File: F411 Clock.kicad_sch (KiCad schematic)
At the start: 0 parts

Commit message: SCH Save: 4 files changed F411 Clock.kicad_prl 105/0/0 F411 Clock.kicad_pro 429/0/1 F411 Clock.kicad_sch 1893/0/3 ~F411 Clock.kicad_sch.lck 1/0/0
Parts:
- added DS1: WC1602A, Display:WC1602A, symbol Display_Character:WC1602A
- added U1: STM32F411CCUx, Package_DFN_QFN:QFN-48-1EP_7x7mm_P0.5mm_EP5.15x5.15mm, symbol MCU_ST_STM32F4:STM32F411CCUx
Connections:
- new net: U1.23 (VSS), U1.35 (VSS), U1.47 (VSS), U1.49 (VSS)

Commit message: SCH Save: 2 files changed F411 Clock.kicad_pro 0/0/1 F411 Clock.kicad_sch 898/0/6
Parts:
- added J1: USB_C_Receptacle_USB2.0_16P, Connector_USB:USB_C_Receptacle_HCTL_HC-TYPE-C-16P-01A, symbol Connector:USB_C_Receptacle_USB2.0_16P
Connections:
- new net: J1.A1 (GND), J1.A12 (GND), J1.B1 (GND), J1.B12 (GND)
- new net: J1.A4 (VBUS), J1.A9 (VBUS), J1.B4 (VBUS), J1.B9 (VBUS)
- new net: J1.A6 (D+), J1.B6 (D+)
- new net: J1.A7 (D-), J1.B7 (D-)
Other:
- moved on the sheet: DS1
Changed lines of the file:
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@@
 	(generator_version "10.0")
 	(paper "A4")
+	(wire
+		(pts
+			(xy 55.88 81.28) (xy 55.88 83.82)
+		)
+		(stroke
+			(width 0)
+			(type default)
+		)
+	)
+	(wire
+		(pts
+			(xy 53.34 76.2) (xy 55.88 76.2)
+		)
+		(stroke
+			(width 0)
+			(type default)
+		)
+	)
+	(wire
+		(pts
+			(xy 53.34 81.28) (xy 55.88 81.28)
+		)
+		(stroke
+			(width 0)
+			(type default)
+		)
+	)
+	(wire
+		(pts
+			(xy 55.88 76.2) (xy 55.88 78.74)
+		)
+		(stroke
+			(width 0)
+			(type default)
+		)
+	)
+	(wire
+		(pts
+			(xy 53.34 83.82) (xy 55.88 83.82)
+		)
+		(stroke
+			(width 0)
+			(type default)
+		)
+	)
+	(wire
+		(pts
+			(xy 53.34 78.74) (xy 55.88 78.74)
+		)
+		(stroke
+			(width 0)
+			(type default)
+		)
+	)
+	(symbol
+		(lib_id "Connector:USB_C_Receptacle_USB2.0_16P")
+		(at 38.1 78.74 0)
+		(unit 1)
+		(body_style 1)
+		(exclude_from_sim no)
+		(in_bom yes)
+		(on_board yes)
+		(in_pos_files yes)
+		(dnp no)
+		(fields_autoplaced yes)
+		(property "Reference" "J1"
+			(at 38.1 55.88 0)
+			(show_name no)
+			(do_not_autoplace no)
+			(effects
+				(font
+					(size 1.27 1.27)
+				)
+			)
+		)
+		(property "Value" "USB_C_Receptacle_USB2.0_16P"
+			(at 38.1 58.42 0)
+			(show_name no)
+			(do_not_autoplace no)
+			(effects
+				(font
+					(size 1.27 1.27)
+				)
+			)
+		)
+		(property "Footprint" "Connector_USB:USB_C_Receptacle_HCTL_HC-TYPE-C-16P-01A"
+			(at 41.91 78.74 0)
+			(hide yes)
+			(show_name no)
+			(do_not_autoplace no)
+			(effects
+				(font
+					(size 1.27 1.27)
+				)
+			)
+		)
+		(property "Datasheet" "https://www.usb.org/sites/default/files/documents/usb_type-c.zip"
+			(at 41.91 78.74 0)
+			(hide yes)
+			(show_name no)
+			(do_not_autoplace no)
+			(effects
+				(font
+					(size 1.27 1.27)
+				)
+			)
+		)
+		(property "Description" "USB 2.0-only 16P Type-C Receptacle connector"
+			(at 38.1 78.74 0)
+			(hide yes)
+			(show_name no)
+			(do_not_autoplace no)
+			(effects
+				(font
+					(size 1.27 1.27)
+				)
+			)
+		)
+		(pin "A12"
+		)
+		(pin "SH"
+		)
+		(pin "A9"
+		)
+		(pin "B4"
+		)
+		(pin "B8"
+		)
+		(pin "A1"
+		)
+		(pin "B7"
+		)
+		(pin "B9"
+		)
+		(pin "A4"
+		)
+		(pin "A8"
+		)
+		(pin "B5"
+		)
+		(pin "B6"
+		)
+		(pin "B12"
+		)
+		(pin "A5"
+		)
+		(pin "A6"
+		)
+		(pin "A7"
+		)
+		(pin "B1"
+		)
+		(instances
+			(project "F411 Clock"
+				(path "/6121eee1-efe8-450c-8a4d-3ee76e069735"
+					(reference "J1")
+					(unit 1)
+				)
+			)
+		)
+	)
 	(symbol
 		(lib_id "Display_Character:WC1602A")
-		(at 194.31 85.09 0)
+		(at 214.63 68.58 0)
 		(unit 1)
 		(body_style 1)
@@
 		(fields_autoplaced yes)
 		(property "Reference" "DS1"
-			(at 196.4533 62.23 0)
+			(at 216.7733 45.72 0)
 			(show_name no)
 			(do_not_autoplace no)
@@
 		)
 		(property "Value" "WC1602A"
-			(at 196.4533 64.77 0)
+			(at 216.7733 48.26 0)
 			(show_name no)
 			(do_not_autoplace no)
@@
 		)
 		(property "Footprint" "Display:WC1602A"
-			(at 194.31 107.95 0)
+			(at 214.63 91.44 0)
 			(hide yes)
 			(show_name no)
@@
 		)
 		(property "Datasheet" "http://www.wincomlcd.com/pdf/WC1602A-SFYLYHTC06.pdf"
-			(at 212.09 85.09 0)
+			(at 232.41 68.58 0)
 			(hide yes)
 			(show_name no)
@@
 		)
 		(property "Description" "LCD 16x2 Alphanumeric , 8 bit parallel bus, 5V VDD"
-			(at 194.31 85.09 0)
-			(hide yes)
-			(show_name no)
+			(at 214.63 68.58 0)
+			(hide yes)
+			(show_name no)

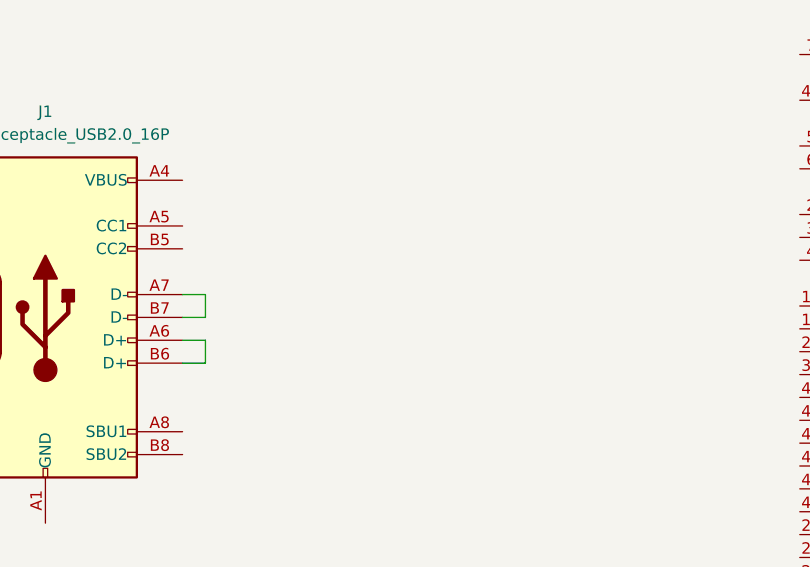
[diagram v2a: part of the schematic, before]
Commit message: SCH Save: 2 files changed F411 Clock.kicad_pro 0/0/1 F411 Clock.kicad_sch 223/0/0
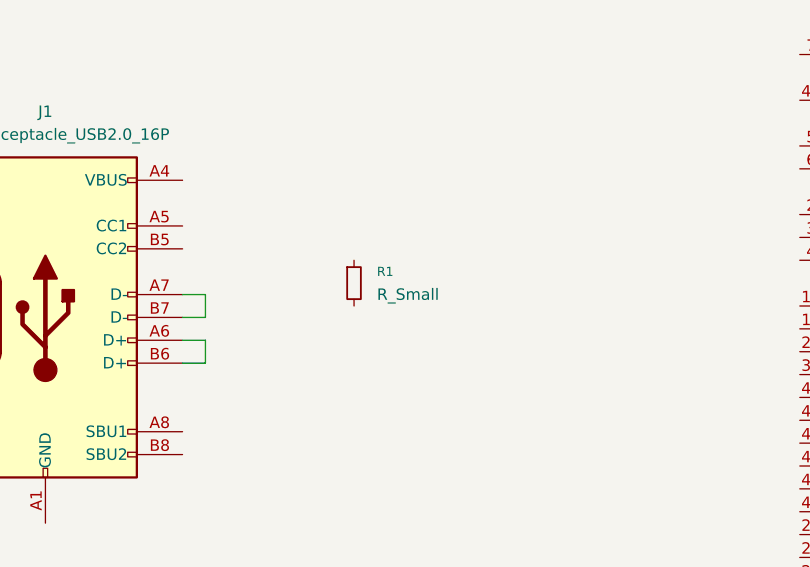
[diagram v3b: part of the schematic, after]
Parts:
- added R1: R_Small, Resistor_SMD:R_0805_2012Metric, symbol Device:R_Small
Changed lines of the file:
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@@
+		)
+	)
+	(symbol
+		(lib_id "Device:R_Small")
+		(at 72.39 74.93 0)
+		(unit 1)
+		(body_style 1)
+		(exclude_from_sim no)
+		(in_bom yes)
+		(on_board yes)
+		(in_pos_files yes)
+		(dnp no)
+		(fields_autoplaced yes)
+		(property "Reference" "R1"
+			(at 74.93 73.6599 0)
+			(show_name no)
+			(do_not_autoplace no)
+			(effects
+				(font
+					(size 1.016 1.016)
+				)
+				(justify left)
+			)
+		)
+		(property "Value" "R_Small"
+			(at 74.93 76.1999 0)
+			(show_name no)
+			(do_not_autoplace no)
+			(effects
+				(font
+					(size 1.27 1.27)
+				)
+				(justify left)
+			)
+		)
+		(property "Footprint" "Resistor_SMD:R_0805_2012Metric"
+			(at 72.39 74.93 0)
+			(hide yes)
+			(show_name no)
+			(do_not_autoplace no)
+			(effects
+				(font
+					(size 1.27 1.27)
+				)
+			)
+		)
+		(property "Datasheet" ""
+			(at 72.39 74.93 0)
+			(hide yes)
+			(show_name no)
+			(do_not_autoplace no)
+			(effects
+				(font
+					(size 1.27 1.27)
+				)
+			)
+		)
+		(property "Description" "Resistor, small symbol"
+			(at 72.39 74.93 0)
+			(hide yes)
+			(show_name no)
+			(do_not_autoplace no)
+			(effects
+				(font
+					(size 1.27 1.27)
+				)
+			)
+		)
+		(pin "2"
+		)
+		(pin "1"
+		)
+		(instances
+			(project "F411 Clock"
+				(path "/6121eee1-efe8-450c-8a4d-3ee76e069735"
+					(reference "R1")
+					(unit 1)
+				)
+			)
 		)
 	)

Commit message: SCH Save: 3 files changed F411 Clock.kicad_prl 11/0/2 F411 Clock.kicad_pro 0/0/1 F411 Clock.kicad_sch 170/0/22
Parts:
- added R2: 10k, Resistor_SMD:R_0805_2012Metric, symbol Device:R_Small
- J1: footprint Connector_USB:USB_C_Receptacle_HCTL_HC-TYPE-C-16P-01A -> Connector_USB:USB_C_Receptacle_GCT_USB4105-xx-A_16P_TopMnt_Horizontal
- R1: value R_Small -> 10k
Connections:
- net at J1.A6 (D+), J1.B6 (D+): now also R2.2
- net at J1.A7 (D-), J1.B7 (D-): now also R1.2
- net DN: now reaches R1.1
- new net DP: R2.1
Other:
- moved on the sheet: J1, R1
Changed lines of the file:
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@@
 	(generator_version "10.0")
 	(paper "A4")
-	(wire
-		(pts
-			(xy 55.88 81.28) (xy 55.88 83.82)
-		)
-		(stroke
-			(width 0)
-			(type default)
-		)
-	)
-	(wire
-		(pts
-			(xy 53.34 76.2) (xy 55.88 76.2)
-		)
-		(stroke
-			(width 0)
-			(type default)
-		)
-	)
-	(wire
-		(pts
-			(xy 53.34 81.28) (xy 55.88 81.28)
-		)
-		(stroke
-			(width 0)
-			(type default)
-		)
-	)
-	(wire
-		(pts
-			(xy 55.88 76.2) (xy 55.88 78.74)
-		)
-		(stroke
-			(width 0)
-			(type default)
-		)
-	)
-	(wire
-		(pts
-			(xy 53.34 83.82) (xy 55.88 83.82)
-		)
-		(stroke
-			(width 0)
-			(type default)
-		)
-	)
-	(wire
-		(pts
-			(xy 53.34 78.74) (xy 55.88 78.74)
-		)
-		(stroke
-			(width 0)
-			(type default)
+	(junction
+		(at 43.18 113.03)
+		(diameter 0)
+		(color 0 0 0 0)
+	)
+	(junction
+		(at 43.18 107.95)
+		(diameter 0)
+		(color 0 0 0 0)
+	)
+	(wire
+		(pts
+			(xy 43.18 111.76) (xy 43.18 113.03)
+		)
+		(stroke
+			(width 0)
+			(type default)
+		)
+	)
+	(wire
+		(pts
+			(xy 40.64 106.68) (xy 43.18 106.68)
+		)
+		(stroke
+			(width 0)
+			(type default)
+		)
+	)
+	(wire
+		(pts
+			(xy 43.18 107.95) (xy 49.53 107.95)
+		)
+		(stroke
+			(width 0)
+			(type default)
+		)
+	)
+	(wire
+		(pts
+			(xy 40.64 111.76) (xy 43.18 111.76)
+		)
+		(stroke
+			(width 0)
+			(type default)
+		)
+	)
+	(wire
+		(pts
+			(xy 43.18 106.68) (xy 43.18 107.95)
+		)
+		(stroke
+			(width 0)
+			(type default)
+		)
+	)
+	(wire
+		(pts
+			(xy 40.64 114.3) (xy 43.18 114.3)
+		)
+		(stroke
+			(width 0)
+			(type default)
+		)
+	)
+	(wire
+		(pts
+			(xy 43.18 113.03) (xy 49.53 113.03)
+		)
+		(stroke
+			(width 0)
+			(type default)
+		)
+	)
+	(wire
+		(pts
+			(xy 43.18 107.95) (xy 43.18 109.22)
+		)
+		(stroke
+			(width 0)
+			(type default)
+		)
+	)
+	(wire
+		(pts
+			(xy 40.64 109.22) (xy 43.18 109.22)
+		)
+		(stroke
+			(width 0)
+			(type default)
+		)
+	)
+	(wire
+		(pts
+			(xy 43.18 113.03) (xy 43.18 114.3)
+		)
+		(stroke
+			(width 0)
+			(type default)
+		)
+	)
+	(wire
+		(pts
+			(xy 54.61 113.03) (xy 58.42 113.03)
+		)
+		(stroke
+			(width 0)
+			(type default)
+		)
+	)
+	(wire
+		(pts
+			(xy 54.61 107.95) (xy 58.42 107.95)
+		)
+		(stroke
+			(width 0)
+			(type default)
+		)
+	)
+	(label "DP"
+		(at 58.42 113.03 0)
+		(effects
+			(font
+				(size 1.27 1.27)
+			)
+			(justify left bottom)
+		)
+	)
+	(label "DN"
+		(at 58.42 107.95 0)
+		(effects
+			(font
+				(size 1.27 1.27)
+			)
+			(justify left bottom)
 		)
 	)
 	(symbol
 		(lib_id "Connector:USB_C_Receptacle_USB2.0_16P")
-		(at 38.1 78.74 0)
+		(at 25.4 109.22 0)
 		(unit 1)
 		(body_style 1)
@@
 		(fields_autoplaced yes)
 		(property "Reference" "J1"
-			(at 38.1 55.88 0)
+			(at 25.4 86.36 0)
 			(show_name no)
 			(do_not_autoplace no)
@@
 		)
 		(property "Value" "USB_C_Receptacle_USB2.0_16P"
-			(at 38.1 58.42 0)
-			(show_name no)
-			(do_not_autoplace no)
-			(effects
-				(font
-					(size 1.27 1.27)
-				)
-			)
-		)
-		(property "Footprint" "Connector_USB:USB_C_Receptacle_HCTL_HC-TYPE-C-16P-01A"
-			(at 41.91 78.74 0)
+			(at 25.4 88.9 0)
+			(show_name no)
+			(do_not_autoplace no)
+			(effects
+				(font
+					(size 1.27 1.27)
+				)
+			)
+		)
+		(property "Footprint" "Connector_USB:USB_C_Receptacle_GCT_USB4105-xx-A_16P_TopMnt_Horizontal"
+			(at 29.21 109.22 0)
 			(hide yes)
 			(show_name no)
@@
 		)
 		(property "Datasheet" "https://www.usb.org/sites/default/files/documents/usb_type-c.zip"
-			(at 41.91 78.74 0)
+			(at 29.21 109.22 0)
 			(hide yes)
 			(show_name no)
@@
 		)
 		(property "Description" "USB 2.0-only 16P Type-C Receptacle connector"
-			(at 38.1 78.74 0)
+			(at 25.4 109.22 0)
 			(hide yes)
 			(show_name no)
@@
 				(path "/6121eee1-efe8-450c-8a4d-3ee76e069735"
 					(reference "J1")
+					(unit 1)
+				)
+			)
+		)
+	)
+	(symbol
+		(lib_id "Device:R_Small")
+		(at 52.07 113.03 270)
+		(mirror x)
+		(unit 1)
+		(body_style 1)
+		(exclude_from_sim no)
+		(in_bom yes)
+		(on_board yes)
+		(in_pos_files yes)
+		(dnp no)
+		(property "Reference" "R2"
+			(at 52.07 118.11 90)
+			(show_name no)
+			(do_not_autoplace no)
+			(effects
+				(font
+					(size 1.016 1.016)
+				)
+			)
+		)
+		(property "Value" "10k"
+			(at 52.07 115.57 90)
+			(show_name no)
+			(do_not_autoplace no)
+			(effects
+				(font
+					(size 1.27 1.27)
+				)
+			)
+		)
+		(property "Footprint" "Resistor_SMD:R_0805_2012Metric"
+			(at 52.07 113.03 0)
+			(hide yes)
+			(show_name no)
+			(do_not_autoplace no)
+			(effects
+				(font
+					(size 1.27 1.27)
+				)
+			)
+		)
+		(property "Datasheet" ""
+			(at 52.07 113.03 0)
+			(hide yes)
+			(show_name no)
+			(do_not_autoplace no)
+			(effects
+				(font
+					(size 1.27 1.27)
+				)
+			)
+		)
+		(property "Description" "Resistor, small symbol"
+			(at 52.07 113.03 0)
+			(hide yes)
+			(show_name no)
+			(do_not_autoplace no)
+			(effects
+				(font
+					(size 1.27 1.27)
+				)
+			)
+		)
+		(pin "2"
+		)
+		(pin "1"
+		)
+		(instances
+			(project "F411 Clock"
+				(path "/6121eee1-efe8-450c-8a4d-3ee76e069735"
+					(reference "R2")
 					(unit 1)
 				)
@@
 	(symbol
 		(lib_id "Device:R_Small")
-		(at 72.39 74.93 0)
+		(at 52.07 107.95 270)
 		(unit 1)
 		(body_style 1)
@@
 		(fields_autoplaced yes)
 		(property "Reference" "R1"
-			(at 74.93 73.6599 0)
+			(at 52.07 102.87 90)
 			(show_name no)
 			(do_not_autoplace no)
@@
 					(size 1.016 1.016)
 				)
-				(justify left)
-			)
-		)
-		(property "Value" "R_Small"
-			(at 74.93 76.1999 0)
-			(show_name no)
-			(do_not_autoplace no)
-			(effects
-				(font
-					(size 1.27 1.27)
-				)
-				(justify left)
+			)
+		)
+		(property "Value" "10k"
+			(at 52.07 105.41 90)
+			(show_name no)
+			(do_not_autoplace no)
+			(effects
+				(font
+					(size 1.27 1.27)
+				)
 			)
 		)
 		(property "Footprint" "Resistor_SMD:R_0805_2012Metric"
-			(at 72.39 74.93 0)
+			(at 52.07 107.95 0)
 			(hide yes)
 			(show_name no)
@@
 		)
 		(property "Datasheet" ""
-			(at 72.39 74.93 0)
+			(at 52.07 107.95 0)
 			(hide yes)
 			(show_name no)
@@
 		)
 		(property "Description" "Resistor, small symbol"
-			(at 72.39 74.93 0)
-			(hide yes)
-			(show_name no)
+			(at 52.07 107.95 0)
+			(hide yes)
+			(show_name no)

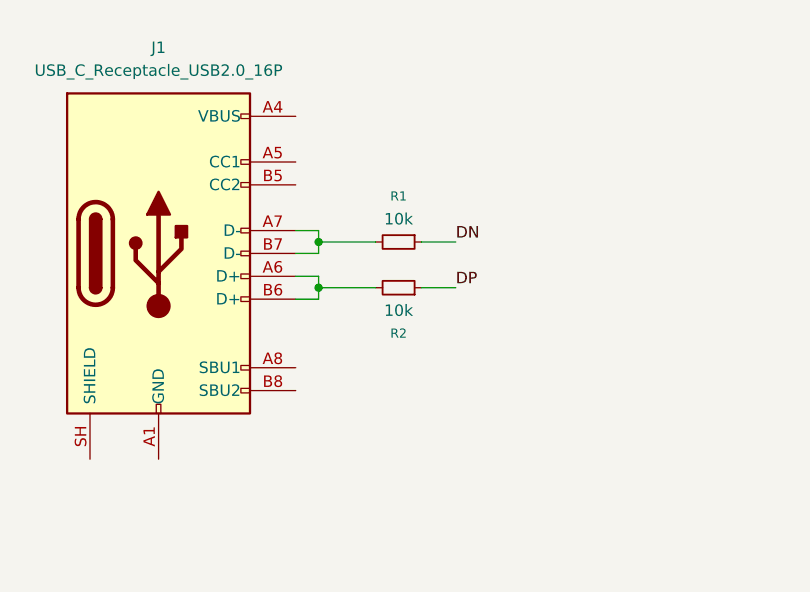
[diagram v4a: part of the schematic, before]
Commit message: SCH Save: 2 files changed F411 Clock.kicad_pro 0/0/1 F411 Clock.kicad_sch 461/0/21
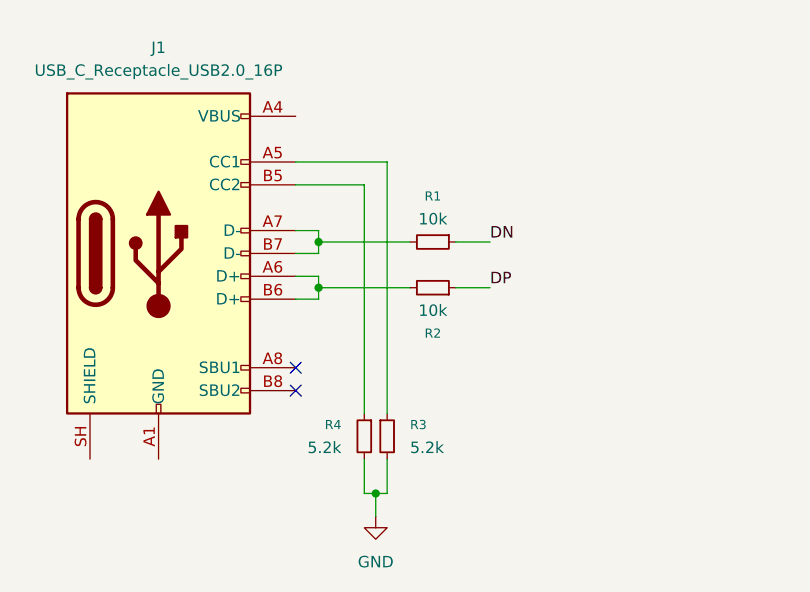
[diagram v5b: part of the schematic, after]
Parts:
- added R3, R4: 5.2k, Resistor_SMD:R_0805_2012Metric, symbol Device:R_Small
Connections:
- net at J1.A5 (CC1): now also R3.1
- net at J1.B5 (CC2): now also R4.1
- new net GND: R3.2, R4.2
- no-connect marks 0 -> 2
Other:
- moved on the sheet: R1, R2

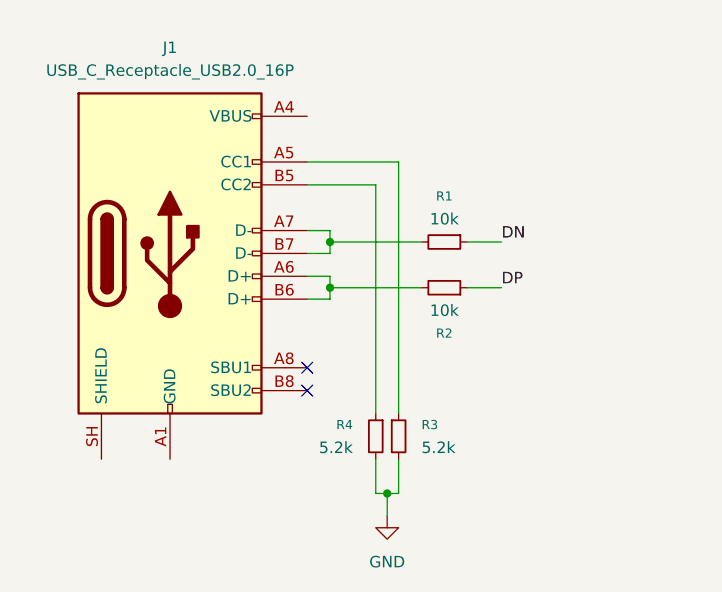
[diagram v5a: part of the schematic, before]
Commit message: SCH Save: 2 files changed F411 Clock.kicad_pro 0/0/1 F411 Clock.kicad_sch 218/0/60
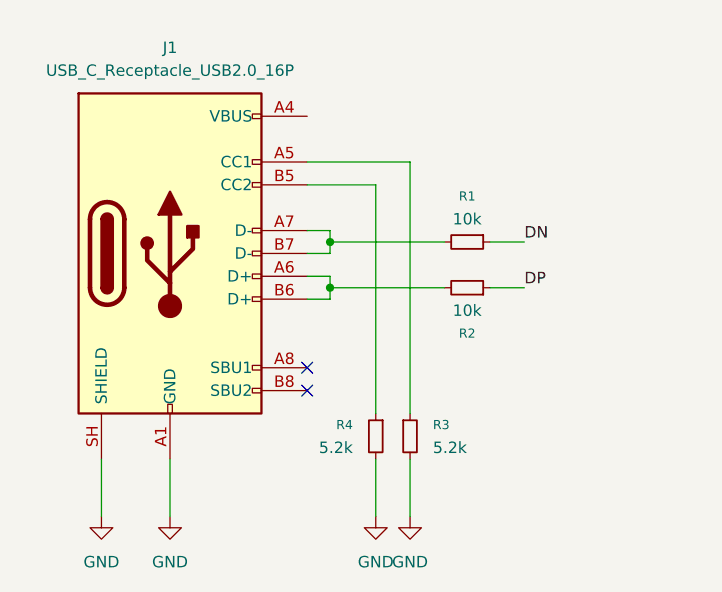
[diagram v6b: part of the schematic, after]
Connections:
- net GND: now also J1.A1 (GND), J1.A12 (GND), J1.B1 (GND), J1.B12 (GND), J1.SH (SHIELD)
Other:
- moved on the sheet: R1, R2, R3

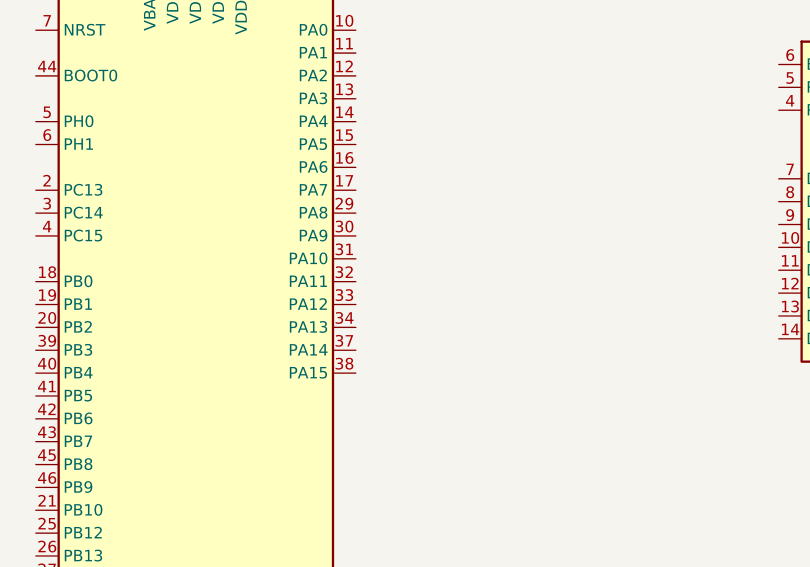
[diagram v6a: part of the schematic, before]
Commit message: SCH Save: 1 files changed F411 Clock.kicad_sch 40/0/0
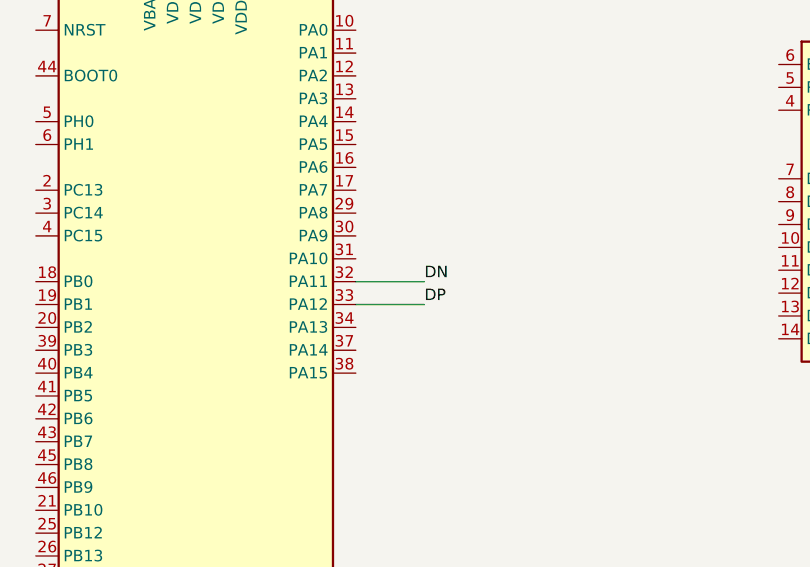
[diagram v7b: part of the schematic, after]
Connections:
- net DN: now also U1.32 (PA11)
- net DP: now also U1.33 (PA12)
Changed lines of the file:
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@@
+	(wire
+		(pts
+			(xy 157.48 80.01) (xy 165.1 80.01)
+		)
+		(stroke
+			(width 0)
+			(type default)
+		)
+	)
 	(wire
 		(pts
@@
 		)
 	)
+	(wire
+		(pts
+			(xy 157.48 77.47) (xy 165.1 77.47)
+		)
+		(stroke
+			(width 0)
+			(type default)
+		)
+	)
+	(label "DP"
+		(at 165.1 80.01 0)
+		(effects
+			(font
+				(size 1.27 1.27)
+			)
+			(justify left bottom)
+		)
+	)
+	(label "DN"
+		(at 165.1 77.47 0)
+		(effects
+			(font
+				(size 1.27 1.27)
+			)
+			(justify left bottom)
+		)
+	)
